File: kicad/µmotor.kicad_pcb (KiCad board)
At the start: 2 copper layers, 20 x 20 mm, 31 parts, among them J101 CAN+PWR, J201 TX, J202 RX, J203 SWDIO, J204 SWCLK, J205 GND, J501 1, J502 2, U201 STM32F042F6Px, U301 MCP1700T-3002E/TT, U401 AS5045B, U501 DRV8870, U502 INA180A1, U601 TCAN330

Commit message: layout: components placed
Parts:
- removed C501: NC, Capacitors_SMD:C_0603
- removed D401: Red, LEDs:LED_0603
- removed D402: Yellow, LEDs:LED_0603
- removed J205: GND, Measurement_Points:Measurement_Point_Round-SMD-Pad_Small
- removed R101: 100k, Resistors_SMD:R_0603
- removed R401, R402: 1k, Resistors_SMD:R_0603
- removed R501: 150m, Resistors_SMD:R_0805
- removed R502: 0, Resistors_SMD:R_0603
- removed U502: INA180A1, TO_SOT_Packages_SMD:SOT-23-5
- added C102: 1µ 6V3, Capacitors_SMD:C_0603, B.Cu at (155.2, 88.0)
- added C304: 1µ 16V X7R, Capacitors_SMD:C_0603, F.Cu at (165.7, 96.5)
- added C305: 47n 50V X7R, Capacitors_SMD:C_0603, F.Cu at (163.0, 96.3)
- added C602: 100n, Capacitors_SMD:C_0603, F.Cu at (158.5, 98.4)
- added D202: Yellow, LEDs:LED_0603, B.Cu at (162.5, 93.6)
- added D601: Blue, LEDs:LED_0603, F.Cu at (163.0, 97.5)
- added D602: Red, LEDs:LED_0603, F.Cu at (161.4, 98.8)
- added J102: U, Measurement_Points:Measurement_Point_Round-TH_Small, F.Cu at (168.3, 86.4)
- added J103: V, Measurement_Points:Measurement_Point_Round-TH_Small, F.Cu at (163.8, 82.0)
- added J104: W, Measurement_Points:Measurement_Point_Round-TH_Small, F.Cu at (157.5, 81.3)
- added J105: U, Measurement_Point_Round-SMD-Pad_Smaller:Measurement_Point_Round-SMD-Pad_Smaller_0.75mm, B.Cu at (160.5, 93.5)
- added J106: V, Measurement_Point_Round-SMD-Pad_Smaller:Measurement_Point_Round-SMD-Pad_Smaller_0.75mm, B.Cu at (159.5, 93.5)
- added J107: W, Measurement_Point_Round-SMD-Pad_Smaller:Measurement_Point_Round-SMD-Pad_Smaller_0.75mm, B.Cu at (158.5, 93.5)
- added J503: 3V3, Measurement_Point_Round-SMD-Pad_Smaller:Measurement_Point_Round-SMD-Pad_Smaller_0.75mm, B.Cu at (160.0, 98.4)
- added J504: GND, Measurement_Point_Round-SMD-Pad_Smaller:Measurement_Point_Round-SMD-Pad_Smaller_0.75mm, B.Cu at (157.0, 98.4)
- added J601: GND, Measurement_Point_Round-SMD-Pad_Smaller:Measurement_Point_Round-SMD-Pad_Smaller_0.75mm, F.Cu at (165.0, 98.0)
- added J602: SWCLK, Measurement_Point_Round-SMD-Pad_Smaller:Measurement_Point_Round-SMD-Pad_Smaller_0.5mm, F.Cu at (159.1, 88.9)
- added J603: SWDIO, Measurement_Point_Round-SMD-Pad_Smaller:Measurement_Point_Round-SMD-Pad_Smaller_0.5mm, F.Cu at (160.7, 91.6)
- added J604: TX, Measurement_Point_Round-SMD-Pad_Smaller:Measurement_Point_Round-SMD-Pad_Smaller_0.5mm, F.Cu at (152.4, 95.9)
- added Q301: FDMD82xx, DFN-12-2EP_3.3x5mm_Pitch0.65mm:DFN-12-2EP_3.3x5mm_Pitch0.65mm, F.Cu at (156.0, 84.1)
- added Q302: FDMD82xx, DFN-12-2EP_3.3x5mm_Pitch0.65mm:DFN-12-2EP_3.3x5mm_Pitch0.65mm, F.Cu at (161.0, 82.8)
- added Q303: FDMD82xx, DFN-12-2EP_3.3x5mm_Pitch0.65mm:DFN-12-2EP_3.3x5mm_Pitch0.65mm, F.Cu at (165.4, 85.2)
- added R202: 1k, Resistors_SMD:R_0603, B.Cu at (164.7, 93.1)
- added R301: 5m, Resistors_SMD:R_0603, F.Cu at (159.6, 86.6)
- added R302: 5m, Resistors_SMD:R_0603, F.Cu at (162.1, 86.0)
- added R303: 5m, Resistors_SMD:R_0603, F.Cu at (162.1, 87.4)
- added R601: 1k, Resistors_SMD:R_0603, B.Cu at (163.0, 96.9)
- added R602: 1k, Resistors_SMD:R_0603, B.Cu at (153.3, 92.8)
- added TP601: ~RST, Measurement_Point_Round-SMD-Pad_Smaller:Measurement_Point_Round-SMD-Pad_Smaller_0.5mm, F.Cu at (152.3, 93.3)
- added TP602: BK, Measurement_Point_Round-SMD-Pad_Smaller:Measurement_Point_Round-SMD-Pad_Smaller_0.5mm, F.Cu at (155.8, 97.7)
- added TP603: DAC, Measurement_Point_Round-SMD-Pad_Smaller:Measurement_Point_Round-SMD-Pad_Smaller_0.5mm, F.Cu at (154.8, 97.7)
- added U101: NCP4623HMX033TCG, Housings_DFN_QFN:DFN-6-1EP_2x2mm_Pitch0.5mm, F.Cu at (154.9, 87.8)
- C101: value 1u -> 1µ 16V; moved to B.Cu
- C201: moved to B.Cu
- C301: value 10µ/10V -> >10µ 35V; footprint Capacitors_SMD:C_0603 -> Capacitors_THT:CP_Radial_D4.0mm_P2.00mm
- C302: value 47µ/35V -> 100n 50V; footprint Capacitors_THT:CP_Radial_D4.0mm_P1.50mm -> Capacitors_SMD:C_0603; moved to B.Cu
- C303: value 10µ/6V3 -> 1µ 6V3 X7R
- D201: value Blue -> Red
- J201: value TX -> A; footprint Measurement_Points:Measurement_Point_Round-SMD-Pad_Small -> Measurement_Point_Round-SMD-Pad_Smaller:Measurement_Point_Round-SMD-Pad_Smaller_0.75mm; moved to B.Cu
- J202: value RX -> B; footprint Measurement_Points:Measurement_Point_Round-SMD-Pad_Small -> Measurement_Point_Round-SMD-Pad_Smaller:Measurement_Point_Round-SMD-Pad_Smaller_0.75mm; moved to B.Cu
- J203: value SWDIO -> 6V; footprint Measurement_Points:Measurement_Point_Round-SMD-Pad_Small -> Measurement_Point_Round-SMD-Pad_Smaller:Measurement_Point_Round-SMD-Pad_Smaller_0.75mm; moved to B.Cu
- J204: value SWCLK -> GND; footprint Measurement_Points:Measurement_Point_Round-SMD-Pad_Small -> Measurement_Point_Round-SMD-Pad_Smaller:Measurement_Point_Round-SMD-Pad_Smaller_0.75mm; moved to B.Cu
- J501: value 1 -> SCL; footprint Measurement_Points:Measurement_Point_Round-SMD-Pad_Small -> Measurement_Point_Round-SMD-Pad_Smaller:Measurement_Point_Round-SMD-Pad_Smaller_0.75mm; moved to B.Cu
- J502: value 2 -> SDA; footprint Measurement_Points:Measurement_Point_Round-SMD-Pad_Small -> Measurement_Point_Round-SMD-Pad_Smaller:Measurement_Point_Round-SMD-Pad_Smaller_0.75mm; moved to B.Cu
- U201: value STM32F042F6Px -> AS5045B; footprint Housings_SSOP:TSSOP-20_4.4x6.5mm_Pitch0.65mm -> Housings_SSOP:SSOP-16_4.4x5.2mm_Pitch0.65mm; moved to B.Cu
- U301: value MCP1700T-3002E/TT -> DRV8323S; footprint TO_SOT_Packages_SMD:SOT-23 -> Housings_DFN_QFN:QFN-40-1EP_6x6mm_Pitch0.5mm
- U401: value AS5045B -> TCAN330; footprint Housings_SSOP:SSOP-16_4.4x5.2mm_Pitch0.65mm -> TO_SOT_Packages_SMD:SOT-23-8
- U501: value DRV8870 -> TMP006; footprint HSOP-8:HSOP-8 -> WCSP-8_1.6x1.6mm_P0.5mm:WCSP-8_1.6x1.6mm_P0.5mm; moved to B.Cu
- U601: value TCAN330 -> STM32L433C(B-C)Ux_u; footprint TO_SOT_Packages_SMD:SOT-23-8 -> Housings_DFN_QFN:QFN-48-1EP_7x7mm_Pitch0.5mm
- moved C302 24.3 mm to (154.8, 85.2), turned to 270 degrees
- moved J101 21.7 mm to (151.0, 84.9), turned to 0 degrees
- moved U301 21.5 mm to (165.0, 92.0), turned to 90 degrees
- moved C303 21.5 mm to (160.8, 88.6), turned to 0 degrees
- moved C301 20.3 mm to (152.9, 84.5), turned to 270 degrees
- moved J204 16.5 mm to (159.3, 88.9)
- moved J501 15.2 mm to (158.0, 98.4)
- moved J502 15.0 mm to (159.0, 98.4)
- moved C101 14.0 mm to (153.9, 88.0)
- moved U501 13.6 mm to (159.6, 95.5), turned to 270 degrees
- moved J203 12.3 mm to (153.9, 89.8)
- moved U601 11.1 mm to (156.6, 93.3), turned to 0 degrees
- moved U201 10.9 mm to (160.0, 90.0), turned to 0 degrees
- moved C201 10.9 mm to (164.3, 90.4), turned to 90 degrees
- moved R201 10.8 mm to (166.2, 93.1), turned to 270 degrees
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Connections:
- C101 pad 1: /Motor_Driver/VREF -> +6V
- C301 pad 1: +6V -> +24V
- C303 pad 1: +3V3 -> /Motor_Driver/3V3_DRV
- D201 pad 2: +3V3 -> Net-(D201-Pad2)
- J201 pad 1: Net-(J201-Pad1) -> /Encoder/A
- J202 pad 1: Net-(J202-Pad1) -> /Encoder/B
- J203 pad 1: Net-(J203-Pad1) -> +6V
- J204 pad 1: Net-(J204-Pad1) -> GND
- J501 pad 1: Net-(J501-Pad1) -> /Microcontroller/I2C_SCL
- J502 pad 1: Net-(J502-Pad1) -> /Microcontroller/I2C_SDA
- R201 pad 1: Net-(R201-Pad1) -> +3V3
- R201 pad 2: Net-(D201-Pad1) -> Net-(D201-Pad2)
- U201 pad 1: (no net) -> Net-(D202-Pad1)
- U201 pad 10: /Microcontroller/PWM_TIM14_CH1 -> (no net)
- U201 pad 11: /Microcontroller/ADC -> (no net)
- U201 pad 13: /Motor_Driver/IN2 -> (no net)
- U201 pad 14: /Motor_Driver/IN1 -> (no net)
- U201 pad 15: GND -> +3V3
- U201 pad 2: (no net) -> Net-(D201-Pad1)
- U201 pad 3: Net-(R201-Pad1) -> /Encoder/A
- U201 pad 4: (no net) -> /Encoder/B
- U201 pad 5: +3V3 -> (no net)
- U201 pad 6: /Encoder/A -> (no net)
- U201 pad 7: /Encoder/B -> GND
- U201 pad 8: Net-(J201-Pad1) -> GND
- U201 pad 9: Net-(J202-Pad1) -> (no net)
- U301 pad 1: GND -> /Motor_Driver/CPL
- U301 pad 2: +3V3 -> /Motor_Driver/CPH
- U301 pad 3: +6V -> /Motor_Driver/VCP
- U401 pad 1: Net-(D402-Pad1) -> /CAN/CAN_TX
- U401 pad 2: Net-(D401-Pad1) -> GND
- U401 pad 3: /Encoder/A -> +3V3
- U401 pad 4: /Encoder/B -> /CAN/CAN_RX
- U401 pad 6: (no net) -> /CAN/CAN_L
- U401 pad 7: GND -> /CAN/CAN_H
- U401 pad 8: GND -> (no net)
- U601 pad 1: /CAN/CAN_TX -> +3V3
- U601 pad 2: GND -> (no net)
- U601 pad 3: +3V3 -> (no net)
- U601 pad 4: /CAN/CAN_RX -> (no net)
- U601 pad 5: (no net) -> /Microcontroller/LedRed
- U601 pad 6: /CAN/CAN_L -> (no net)
- U601 pad 7: /CAN/CAN_H -> /Microcontroller/~RST
- U601 pad 8: (no net) -> GND
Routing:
- net +3V3: track 0.00 -> 42.4 mm, vias 0 -> 5
- net GND: track 0.00 -> 28.2 mm, vias 0 -> 7
- net Net-(Q303-Pad4): track 0.00 -> 20.6 mm, vias 0 -> 2
- net /Microcontroller/GpioB2: track 0.00 -> 19.3 mm, vias 0 -> 2
- net /Motor_Driver/ENABLE: track 0.00 -> 17.3 mm, vias 0 -> 2
- net /Microcontroller/SenseV: track 0.00 -> 17.1 mm, vias 0 -> 2
- net /Microcontroller/SenseAll: track 0.00 -> 17.0 mm, vias 0 -> 2
- net /Microcontroller/SenseW: track 0.00 -> 15.8 mm, vias 0 -> 2
- net Net-(Q303-Pad12): track 0.00 -> 15.4 mm, vias 0 -> 2
- net /Motor_Driver/OUT_U: track 0.00 -> 11.8 mm, vias 0 -> 1
- net /Encoder/B: track 0.00 -> 11.6 mm, vias 0 -> 1
- net /Encoder/A: track 0.00 -> 10.7 mm, vias 0 -> 1
- net /Microcontroller/CS: track 0.00 -> 10.2 mm
- net +6V: track 0.00 -> 9.84 mm, vias 0 -> 1
- net /Microcontroller/MOSI: track 0.00 -> 9.70 mm, vias 0 -> 2
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- added copper zone on F.Cu, net +24V
- added copper zone on In1.Cu, net +24V
- added copper zone on F.Cu, net /Motor_Driver/OUT_U
- added copper zone on F.Cu, net /Motor_Driver/OUT_V
- added copper zone on F.Cu, net /Motor_Driver/OUT_W
- added copper zone on In1.Cu, net GND
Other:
- outline, holes or cut-outs redrawn
- copper layers 2 -> 4
- net class Default: clearance 0.2 -> 0.125; trace_width 0.25 -> 0.15; via_dia 0.6 -> 0.45; via_drill 0.4 -> 0.2
- rule pad_to_mask_clearance: 0.05 -> 0
- rule trace_clearance: 0.2 -> 0.125
- rule trace_min: 0.2 -> 0.1
- rule via_min_drill: 0.3 -> 0.2
- rule via_min_size: 0.4 -> 0.45

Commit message: layout: routing finished
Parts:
- moved J105 7.28 mm to (154.2, 89.9)
- moved J106 5.40 mm to (155.4, 89.9)
- moved J107 3.72 mm to (155.4, 91.4)
- moved R303 3.34 mm to (158.8, 87.0)
- moved D202 1.96 mm to (163.0, 95.5)
- moved D201 1.96 mm to (162.5, 93.6)
- moved R201 1.52 mm to (164.7, 93.1)
- moved J204 1.45 mm to (158.1, 88.0)
- moved J202 1.42 mm to (158.2, 89.9)
- moved J201 1.42 mm to (158.2, 90.9)
- moved R202 1.40 mm to (166.1, 93.1)
- moved J203 1.35 mm to (153.0, 88.8)
- moved C303 1.31 mm to (161.0, 89.9), turned to 90 degrees
- moved R301 1.12 mm to (160.8, 86.5)
- moved J102 0.57 mm to (168.0, 85.9)
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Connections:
- U601 pad 32: /Microcontroller/HallV -> /CAN/CAN_RX
- U601 pad 33: /Microcontroller/HallU -> /CAN/CAN_TX
- U601 pad 38: /Microcontroller/HallW -> /Microcontroller/CS
- U601 pad 42: /Microcontroller/CS -> /Microcontroller/HallW
- U601 pad 45: /CAN/CAN_RX -> /Microcontroller/HallV
- U601 pad 46: /CAN/CAN_TX -> /Microcontroller/HallU
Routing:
- net +24V: track 3.18 -> 53.9 mm, vias 0 -> 32
- net GND: track 28.2 -> 67.0 mm, vias 7 -> 20
- net Net-(Q301-Pad12): track 0.00 -> 20.6 mm, vias 0 -> 2
- net Net-(Q302-Pad4): track 0.00 -> 19.2 mm, vias 0 -> 2
- net /Motor_Driver/OUT_W: track 0.00 -> 18.0 mm, vias 0 -> 2
- net Net-(Q302-Pad12): track 0.00 -> 17.0 mm, vias 0 -> 2
- net Net-(Q301-Pad4): track 0.00 -> 16.4 mm, vias 0 -> 2
- net Net-(Q302-Pad14): track 0.00 -> 16.3 mm, vias 0 -> 2
- net /Motor_Driver/OUT_V: track 0.00 -> 14.2 mm, vias 0 -> 2
- net +3V3: track 42.4 -> 56.3 mm, vias 5 -> 6
- net Net-(Q301-Pad14): track 0.00 -> 12.7 mm, vias 0 -> 2
- net /Microcontroller/LedRedR: track 0.00 -> 11.7 mm, vias 0 -> 1
- net Net-(Q303-Pad14): track 1.81 -> 13.0 mm, vias 0 -> 2
- net /Microcontroller/GpioB7: track 0.00 -> 10.8 mm, vias 0 -> 2
- net Net-(D202-Pad1): track 0.00 -> 9.21 mm
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- added copper zone on B.Cu, net +24V
- added copper zone on F.Cu, net GND
- added copper zone on F.Cu, net Net-(Q301-Pad14)
- added copper zone on F.Cu, net Net-(Q302-Pad14)
- added copper zone on F.Cu, net Net-(Q303-Pad14)

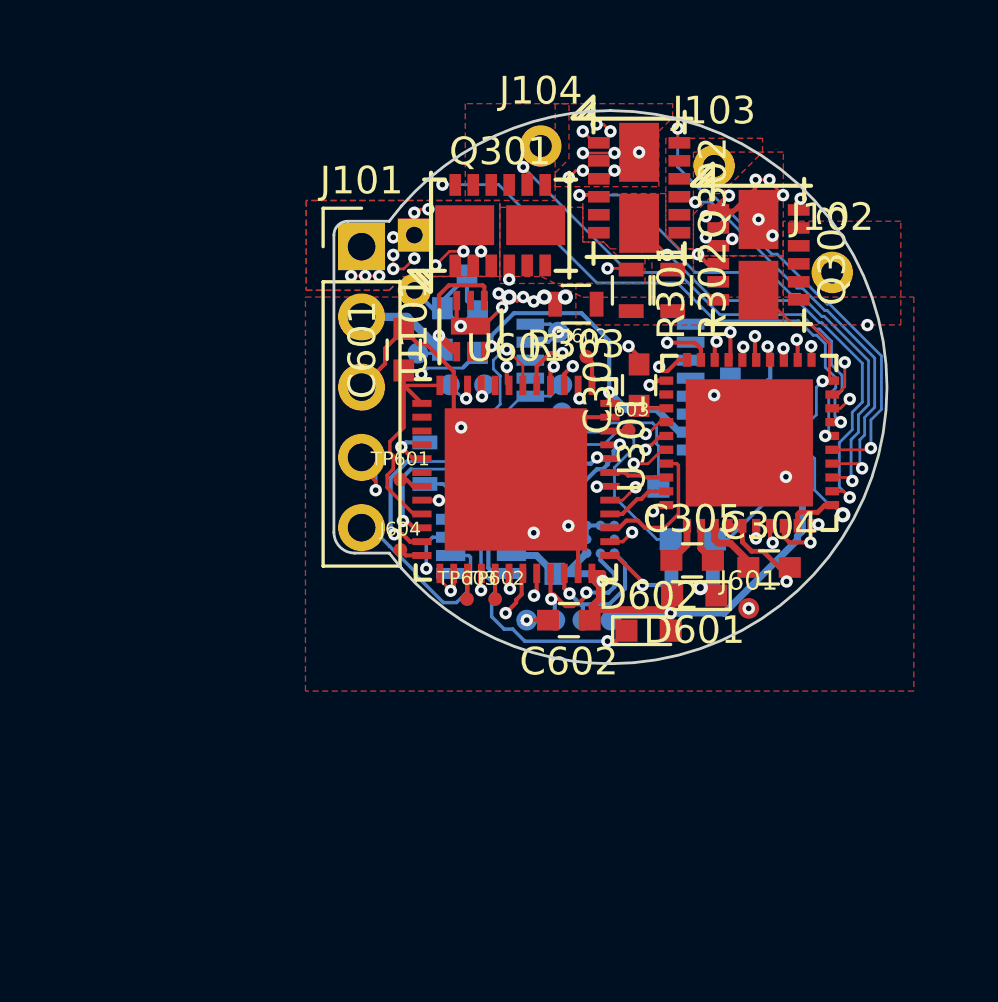
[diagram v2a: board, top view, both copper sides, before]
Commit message: layout: minor improvements
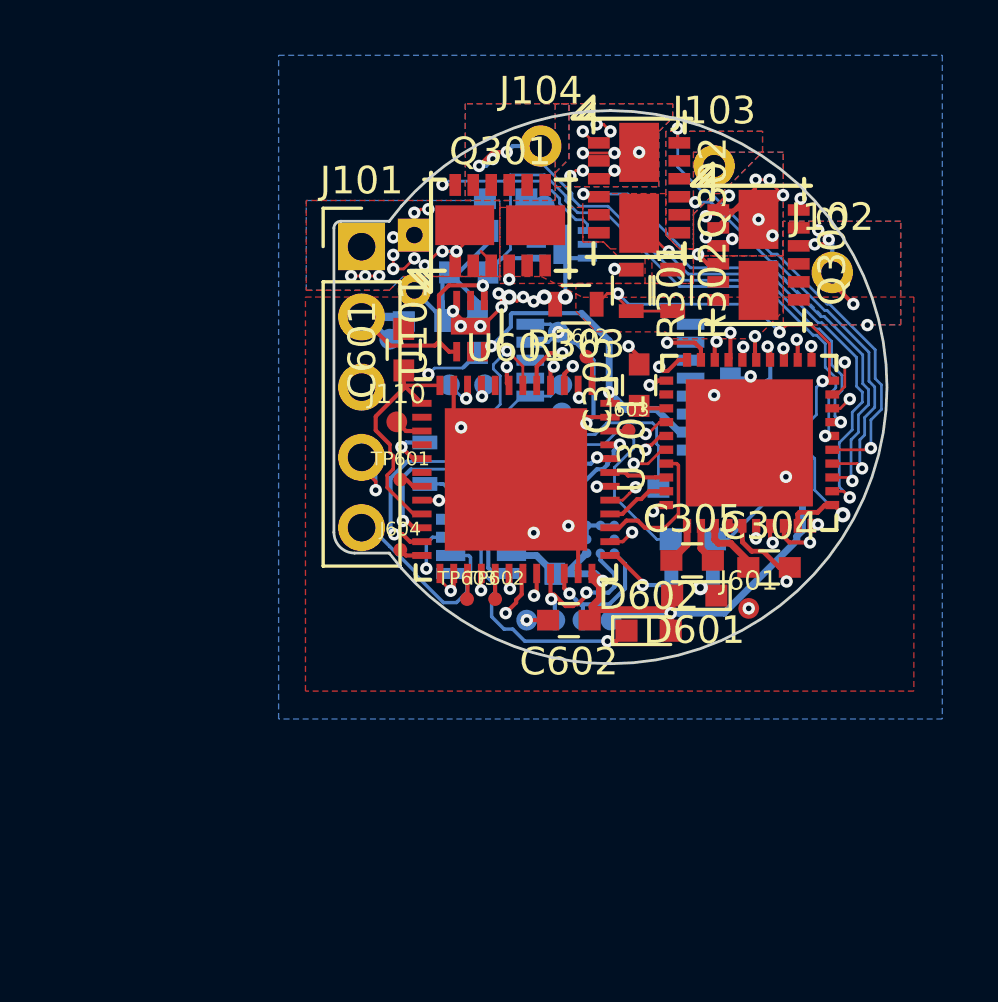
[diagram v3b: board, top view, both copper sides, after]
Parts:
- added C103: 1µ 16V, Capacitors_SMD:C_0603, B.Cu at (155.6, 85.1)
- added C104: 1µ 6V3, Capacitors_SMD:C_0603, B.Cu at (156.2, 83.2)
- added J108: 5V, Measurement_Point_Round-SMD-Pad_Smaller:Measurement_Point_Round-SMD-Pad_Smaller_0.75mm, B.Cu at (157.6, 83.4)
- added J110: IO, Measurement_Point_Round-SMD-Pad_Smaller:Measurement_Point_Round-SMD-Pad_Smaller_0.75mm, F.Cu at (152.3, 91.3)
- added U102: NCP4623HMX050TCG, Housings_DFN_QFN:DFN-6-1EP_2x2mm_Pitch0.5mm, B.Cu at (158.2, 84.8)
- moved J203 1.14 mm to (152.0, 88.3)
- moved C101 0.70 mm to (153.3, 87.6), turned to 0 degrees
- moved C302 0.65 mm to (154.2, 85.1)
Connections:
- U601 pad 3: (no net) -> /Microcontroller/GpioC14
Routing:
- net +6V: track 9.75 -> 21.1 mm
- net Net-(Q303-Pad14): track 13.0 -> 21.5 mm, vias 2 -> 4
- net GND: track 67.0 -> 74.1 mm, vias 20 -> 24
- net /Motor_Driver/OUT_U: track 12.6 -> 17.5 mm, vias 1 -> 5
- net /Motor_Driver/OUT_W: track 18.0 -> 20.6 mm, vias 2 -> 4
- net +5V: track 0.00 -> 2.05 mm
- net /Microcontroller/GpioC14: track 0.00 -> 1.05 mm
- net Net-(Q301-Pad14): track 12.7 -> 12.2 mm
- added copper zone on In2.Cu, net +24V
- added copper zone on B.Cu, net /Motor_Driver/OUT_U
- added copper zone on B.Cu, net /Motor_Driver/OUT_V
- added copper zone on B.Cu, net /Motor_Driver/OUT_W
- added copper zone on B.Cu, net GND
- added copper zone on In2.Cu, net GND
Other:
- outline, holes or cut-outs redrawn

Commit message: layout: improvements and silkscreen
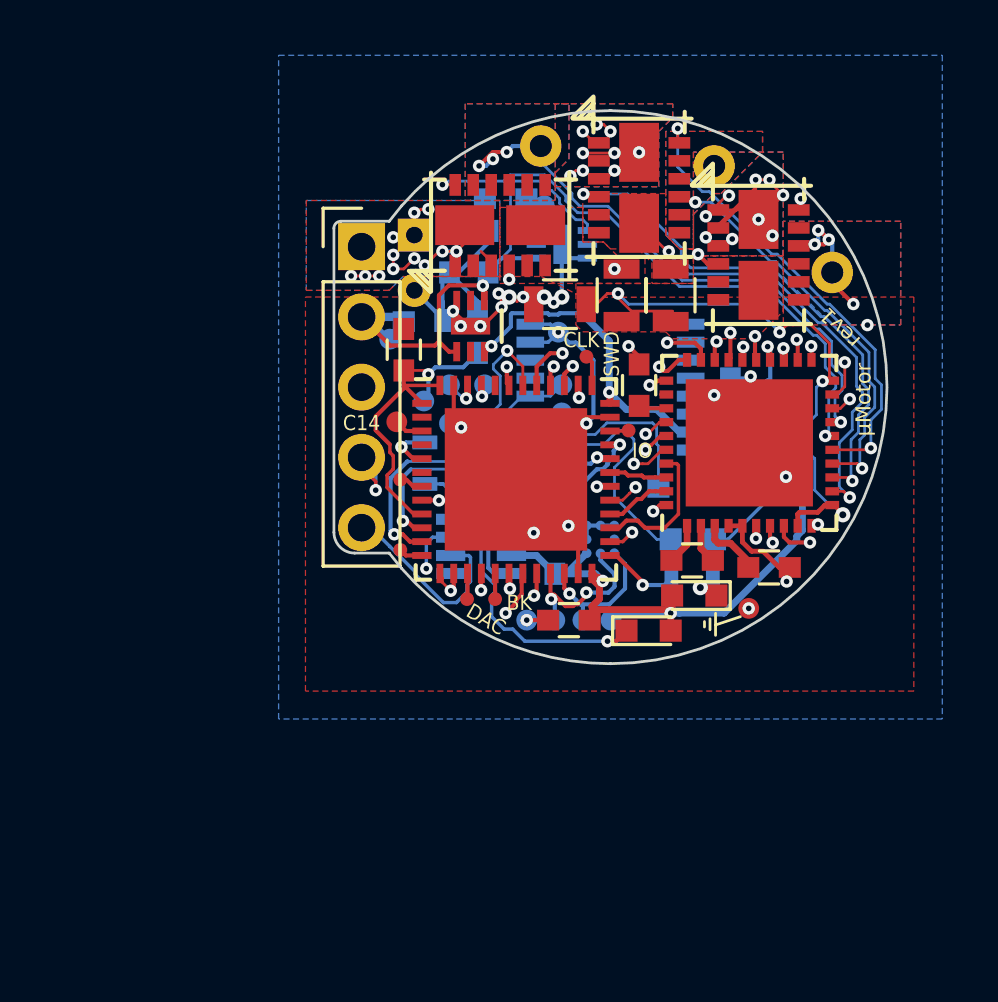
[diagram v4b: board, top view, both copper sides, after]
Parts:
- added J109: 3V3, Measurement_Point_Round-SMD-Pad_Smaller:Measurement_Point_Round-SMD-Pad_Smaller_0.75mm, B.Cu at (153.2, 90.5)
- added J111: GND, Measurement_Point_Round-SMD-Pad_Smaller:Measurement_Point_Round-SMD-Pad_Smaller_0.75mm, B.Cu at (154.2, 91.3)
- R301, R302, R303: footprint Resistors_SMD:R_0603 -> Resistors_SMD:R_0805
- moved R303 0.57 mm to (158.2, 87.0)
- moved R301 0.39 mm to (160.4, 86.7)
- moved R302 0.19 mm to (162.2, 86.7)
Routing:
- net +3V3: track 56.6 -> 57.7 mm
- net GND: track 74.1 -> 75.0 mm
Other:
- board text added: "+"
- board text added: "+5V"
- board text added: "+7V"
- board text added: "A"
- board text added: "B"
- board text added: "BK"
- board text added: "C14"
- board text added: "CLK"
- board text added: "DA CL"
- board text added: "DAC"
- board text added: "DEC"
- board text added: "Hall"
- board text added: "I2C"
- board text added: "INC"
- board text added: "IO"
- board text added: "SWD"
- board text added: "U"
- board text added: "V"
- board text added: "W"
- board text added: "rev1"
- board text added: "rleh 2018"
- board text added: "µMotor"
- board text added: "µMotor rev1"
